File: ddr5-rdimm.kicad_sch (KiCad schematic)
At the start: 31 parts, among them J2 Bus_DDR5_DDR504111002KQ, Q10 BSS138PW, Q11 BSS138PW, Q9 BSS138PW, SW3 SW_KMR211NGLFS_SMD

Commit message: [#65754] Rename project
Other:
- title: SO-DIMM DDR5 Tester -> RDIMM DDR5 Tester

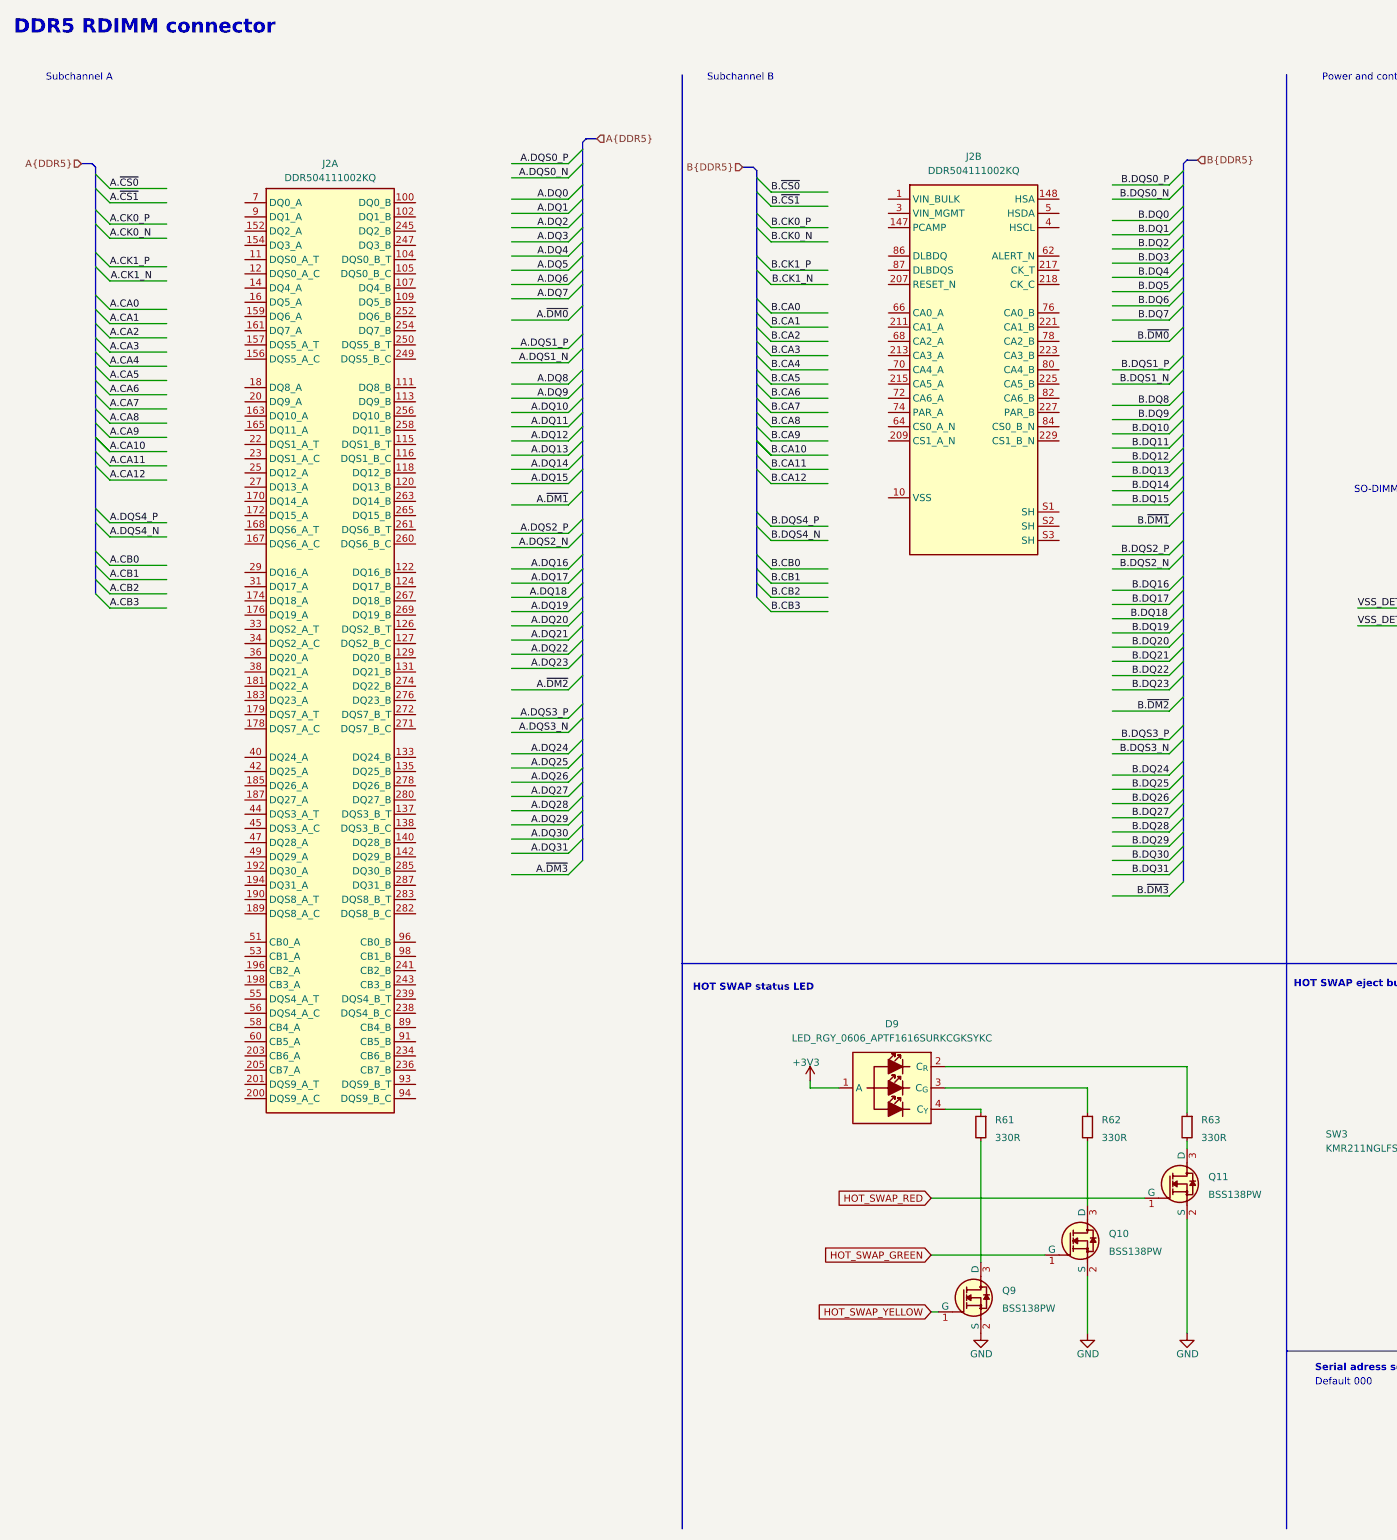
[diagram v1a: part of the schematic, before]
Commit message: [#66521] Connect labels to DDR5 connector - define DDR5_RDIMM bus
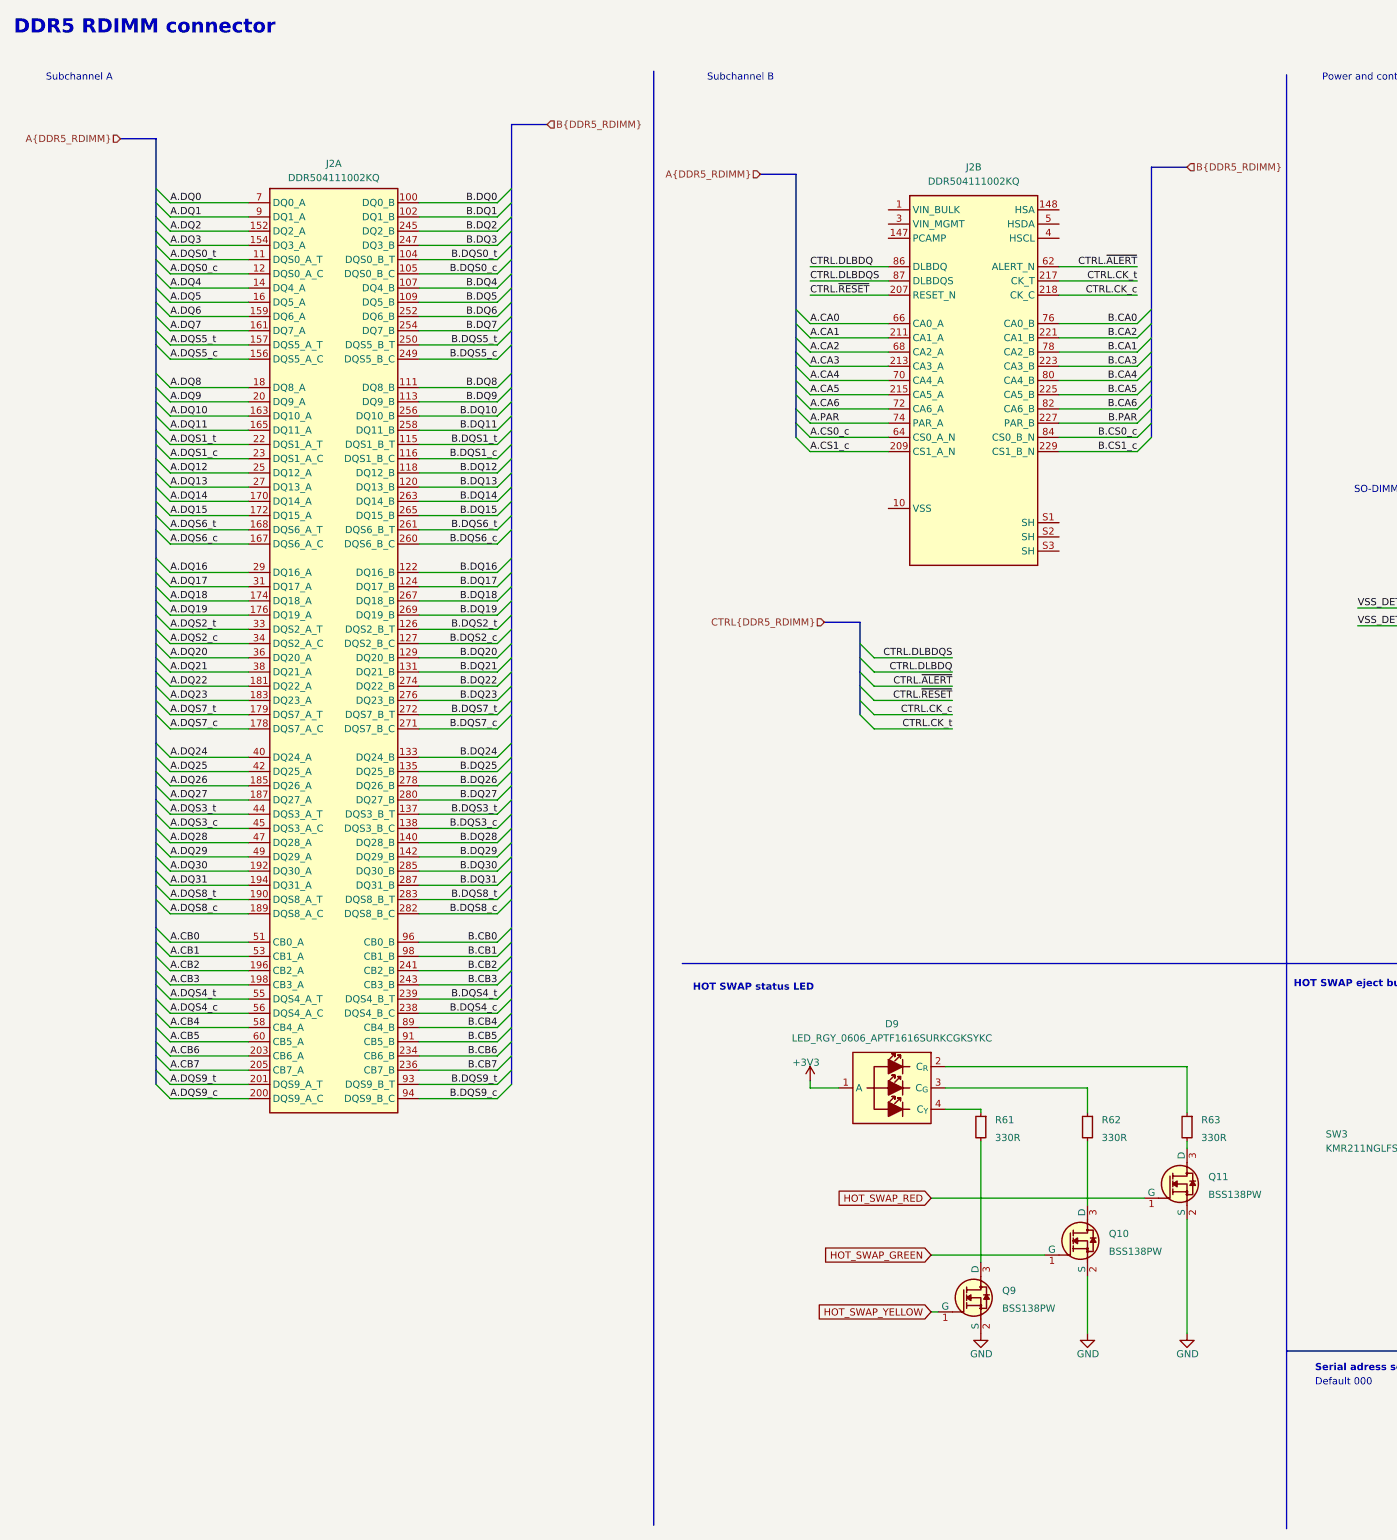
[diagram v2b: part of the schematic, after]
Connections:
- net A.CA0: now also J2.66 (CA0_A)
- net A.CA1: now also J2.211 (CA1_A)
- net A.CA2: now also J2.68 (CA2_A)
- net A.CA3: now also J2.213 (CA3_A)
- net A.CA4: now also J2.70 (CA4_A)
- net A.CA5: now also J2.215 (CA5_A)
- net A.CA6: now also J2.72 (CA6_A)
- net A.CB0: now also J2.51 (CB0_A)
- net A.CB1: now also J2.53 (CB1_A)
- net A.CB2: now also J2.196 (CB2_A)
- net A.CB3: now also J2.198 (CB3_A)
- net A.DQ0: now also J2.7 (DQ0_A)
- net A.DQ1: now also J2.9 (DQ1_A)
- net A.DQ10: now also J2.163 (DQ10_A)
- net A.DQ11: now also J2.165 (DQ11_A)
- net A.DQ12: now also J2.25 (DQ12_A)
- net A.DQ13: now also J2.27 (DQ13_A)
- net A.DQ14: now also J2.170 (DQ14_A)
- net A.DQ15: now also J2.172 (DQ15_A)
- net A.DQ16: now also J2.29 (DQ16_A)
- net A.DQ17: now also J2.31 (DQ17_A)
- net A.DQ18: now also J2.174 (DQ18_A)
- net A.DQ19: now also J2.176 (DQ19_A)
- net A.DQ2: now also J2.152 (DQ2_A)
- net A.DQ20: now also J2.36 (DQ20_A)
- net A.DQ21: now also J2.38 (DQ21_A)
- net A.DQ22: now also J2.181 (DQ22_A)
- net A.DQ23: now also J2.183 (DQ23_A)
- net A.DQ24: now also J2.40 (DQ24_A)
- net A.DQ25: now also J2.42 (DQ25_A)
- net A.DQ26: now also J2.185 (DQ26_A)
- net A.DQ27: now also J2.187 (DQ27_A)
- net A.DQ28: now also J2.47 (DQ28_A)
- net A.DQ29: now also J2.49 (DQ29_A)
- net A.DQ3: now also J2.154 (DQ3_A)
- net A.DQ30: now also J2.192 (DQ30_A)
- net A.DQ31: now also J2.194 (DQ31_A)
- net A.DQ4: now also J2.14 (DQ4_A)
- net A.DQ5: now also J2.16 (DQ5_A)
- net A.DQ6: now also J2.159 (DQ6_A)
- net A.DQ7: now also J2.161 (DQ7_A)
- net A.DQ8: now also J2.18 (DQ8_A)
- net A.DQ9: now also J2.20 (DQ9_A)
- net B.CA0: now also J2.76 (CA0_B)
- net B.CA1: now also J2.78 (CA2_B)
- net B.CA2: now also J2.221 (CA1_B)
- net B.CA3: now also J2.223 (CA3_B)
- net B.CA4: now also J2.80 (CA4_B)
- net B.CA5: now also J2.225 (CA5_B)
- net B.CA6: now also J2.82 (CA6_B)
- net B.CB0: now also J2.96 (CB0_B)
- net B.CB1: now also J2.98 (CB1_B)
- net B.CB2: now also J2.241 (CB2_B)
- net B.CB3: now also J2.243 (CB3_B)
- net B.DQ0: now also J2.100 (DQ0_B)
- net B.DQ1: now also J2.102 (DQ1_B)
- net B.DQ10: now also J2.256 (DQ10_B)
- net B.DQ11: now also J2.258 (DQ11_B)
- net B.DQ12: now also J2.118 (DQ12_B)
- net B.DQ13: now also J2.120 (DQ13_B)
- net B.DQ14: now also J2.263 (DQ14_B)
- net B.DQ15: now also J2.265 (DQ15_B)
- net B.DQ16: now also J2.122 (DQ16_B)
- net B.DQ17: now also J2.124 (DQ17_B)
- net B.DQ18: now also J2.267 (DQ18_B)
- net B.DQ19: now also J2.269 (DQ19_B)
- net B.DQ2: now also J2.245 (DQ2_B)
- net B.DQ20: now also J2.129 (DQ20_B)
- net B.DQ21: now also J2.131 (DQ21_B)
- net B.DQ22: now also J2.274 (DQ22_B)
- net B.DQ23: now also J2.276 (DQ23_B)
- net B.DQ24: now also J2.133 (DQ24_B)
- net B.DQ25: now also J2.135 (DQ25_B)
- net B.DQ26: now also J2.278 (DQ26_B)
- net B.DQ27: now also J2.280 (DQ27_B)
- net B.DQ28: now also J2.140 (DQ28_B)
- net B.DQ29: now also J2.142 (DQ29_B)
- net B.DQ3: now also J2.247 (DQ3_B)
- net B.DQ30: now also J2.285 (DQ30_B)
- net B.DQ31: now also J2.287 (DQ31_B)
- net B.DQ4: now also J2.107 (DQ4_B)
- net B.DQ5: now also J2.109 (DQ5_B)
- net B.DQ6: now also J2.252 (DQ6_B)
- net B.DQ7: now also J2.254 (DQ7_B)
- net B.DQ8: now also J2.111 (DQ8_B)
- net B.DQ9: now also J2.113 (DQ9_B)
- net B.DQS0_t: now reaches J2.104 (DQS0_B_T)
- net B.DQS0_c: now reaches J2.105 (DQS0_B_C)
- net A.DQS0_t: now reaches J2.11 (DQS0_A_T)
- net B.DQS1_t: now reaches J2.115 (DQS1_B_T)
- net B.DQS1_c: now reaches J2.116 (DQS1_B_C)
- net A.DQS0_c: now reaches J2.12 (DQS0_A_C)
- net B.DQS2_t: now reaches J2.126 (DQS2_B_T)
- net B.DQS2_c: now reaches J2.127 (DQS2_B_C)
- net B.DQS3_t: now reaches J2.137 (DQS3_B_T)
- net B.DQS3_c: now reaches J2.138 (DQS3_B_C)
- net A.DQS5_c: now reaches J2.156 (DQS5_A_C)
- net A.DQS5_t: now reaches J2.157 (DQS5_A_T)
- net A.DQS6_c: now reaches J2.167 (DQS6_A_C)
- net A.DQS6_t: now reaches J2.168 (DQS6_A_T)
- net A.DQS7_c: now reaches J2.178 (DQS7_A_C)
- net A.DQS7_t: now reaches J2.179 (DQS7_A_T)
- net A.DQS8_c: now reaches J2.189 (DQS8_A_C)
- net A.DQS8_t: now reaches J2.190 (DQS8_A_T)
- net A.DQS9_c: now reaches J2.200 (DQS9_A_C)
- net A.DQS9_t: now reaches J2.201 (DQS9_A_T)
- net A.CB6: now reaches J2.203 (CB6_A)
- net A.CB7: now reaches J2.205 (CB7_A)
- net A.DQS1_t: now reaches J2.22 (DQS1_A_T)
- net A.DQS1_c: now reaches J2.23 (DQS1_A_C)
- net B.CB6: now reaches J2.234 (CB6_B)
- net B.CB7: now reaches J2.236 (CB7_B)
- net B.DQS4_c: now reaches J2.238 (DQS4_B_C)
- net B.DQS4_t: now reaches J2.239 (DQS4_B_T)
- net B.DQS5_c: now reaches J2.249 (DQS5_B_C)
- net B.DQS5_t: now reaches J2.250 (DQS5_B_T)
- net B.DQS6_c: now reaches J2.260 (DQS6_B_C)
- net B.DQS6_t: now reaches J2.261 (DQS6_B_T)
- net B.DQS7_c: now reaches J2.271 (DQS7_B_C)
- net B.DQS7_t: now reaches J2.272 (DQS7_B_T)
- net B.DQS8_c: now reaches J2.282 (DQS8_B_C)
- net B.DQS8_t: now reaches J2.283 (DQS8_B_T)
- net A.DQS2_t: now reaches J2.33 (DQS2_A_T)
- net A.DQS2_c: now reaches J2.34 (DQS2_A_C)
- net A.DQS3_t: now reaches J2.44 (DQS3_A_T)
- net A.DQS3_c: now reaches J2.45 (DQS3_A_C)
- net A.DQS4_t: now reaches J2.55 (DQS4_A_T)
- net A.DQS4_c: now reaches J2.56 (DQS4_A_C)
- net A.CB4: now reaches J2.58 (CB4_A)
- net A.CB5: now reaches J2.60 (CB5_A)
- net B.CB4: now reaches J2.89 (CB4_B)
- net B.CB5: now reaches J2.91 (CB5_B)
- net B.DQS9_t: now reaches J2.93 (DQS9_B_T)
- net B.DQS9_c: now reaches J2.94 (DQS9_B_C)
- net CTRL.~{RESET}: now reaches J2.207 (RESET_N)
- net A.CS1_c: now reaches J2.209 (CS1_A_N)
- net CTRL.CK_t: now reaches J2.217 (CK_T)
- net CTRL.CK_c: now reaches J2.218 (CK_C)
- net B.PAR: now reaches J2.227 (PAR_B)
- net B.CS1_c: now reaches J2.229 (CS1_B_N)
- net CTRL.~{ALERT}: now reaches J2.62 (ALERT_N)
- net A.CS0_c: now reaches J2.64 (CS0_A_N)
- net A.PAR: now reaches J2.74 (PAR_A)
- net B.CS0_c: now reaches J2.84 (CS0_B_N)
- net CTRL.DLBDQ: now reaches J2.86 (DLBDQ)
- net CTRL.DLBDQS: now reaches J2.87 (DLBDQS)
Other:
- moved on the sheet: J2A, J2B

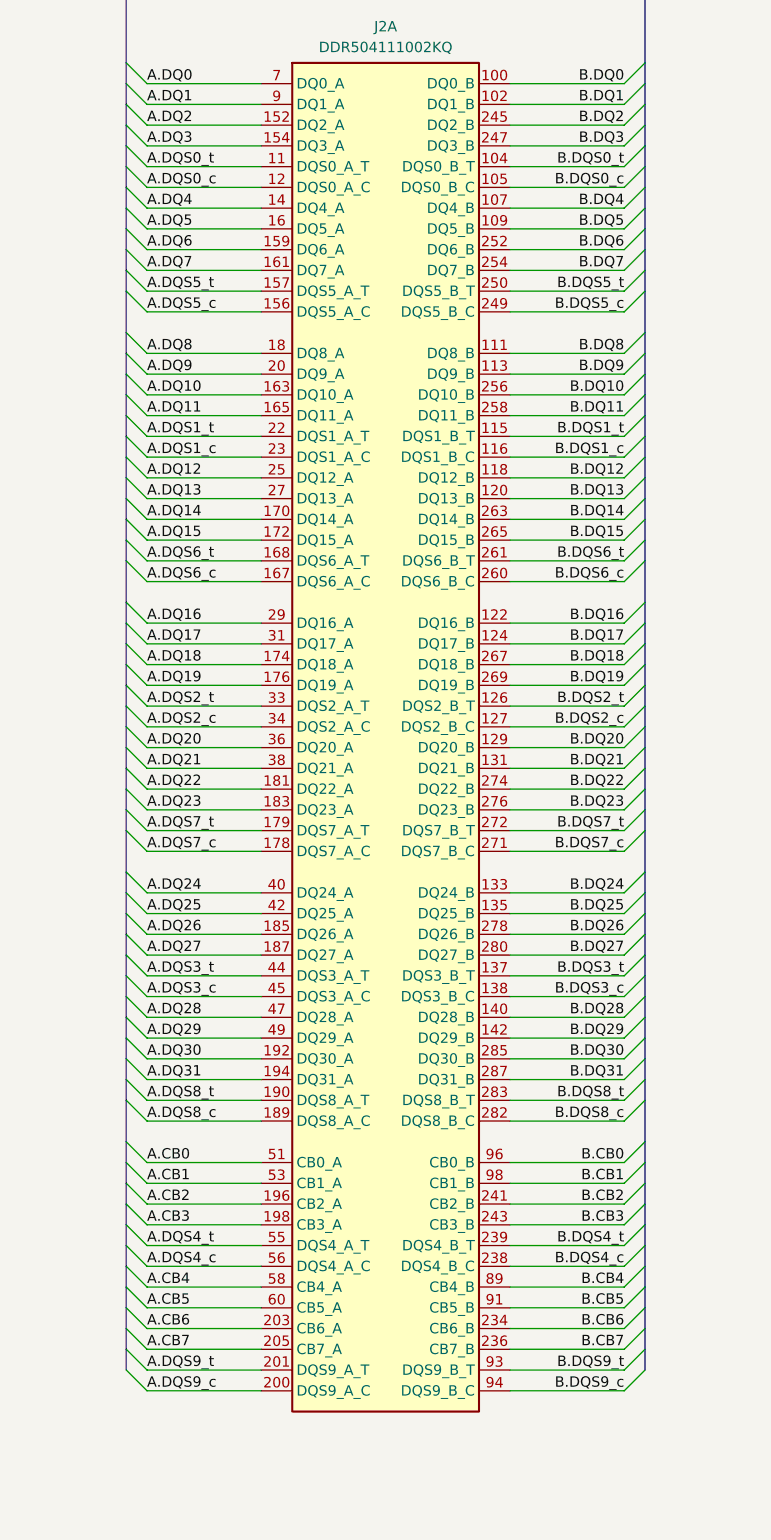
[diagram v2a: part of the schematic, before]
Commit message: [#66521] Rename DQS pairs
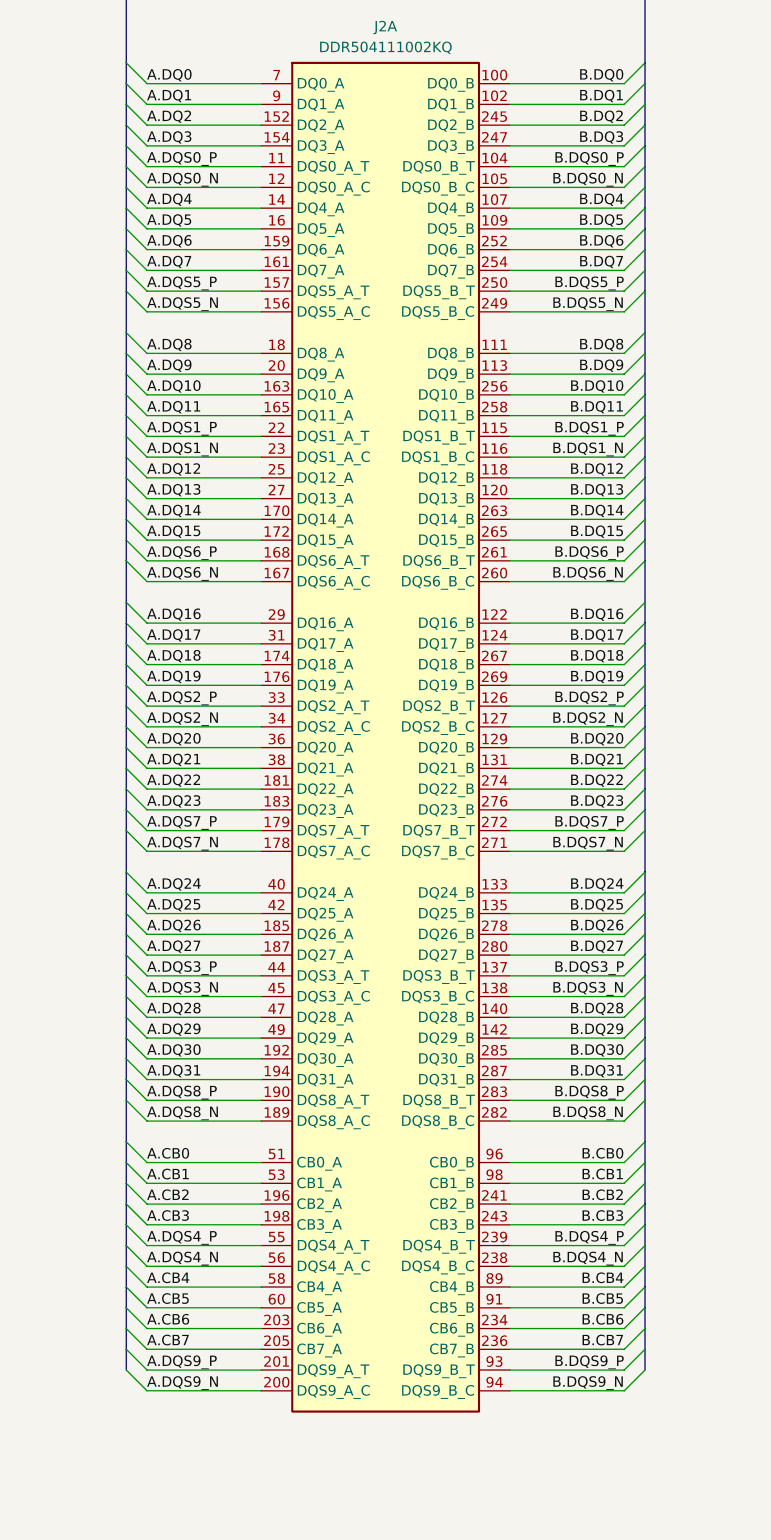
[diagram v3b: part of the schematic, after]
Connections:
- net A.DQS0_c renamed A.DQS0_N
- net A.DQS0_t renamed A.DQS0_P
- net A.DQS1_c renamed A.DQS1_N
- net A.DQS1_t renamed A.DQS1_P
- net A.DQS2_c renamed A.DQS2_N
- net A.DQS2_t renamed A.DQS2_P
- net A.DQS3_c renamed A.DQS3_N
- net A.DQS3_t renamed A.DQS3_P
- net A.DQS4_c renamed A.DQS4_N
- net A.DQS4_t renamed A.DQS4_P
- net A.DQS5_c renamed A.DQS5_N
- net A.DQS5_t renamed A.DQS5_P
- net A.DQS6_c renamed A.DQS6_N
- net A.DQS6_t renamed A.DQS6_P
- net A.DQS7_c renamed A.DQS7_N
- net A.DQS7_t renamed A.DQS7_P
- net A.DQS8_c renamed A.DQS8_N
- net A.DQS8_t renamed A.DQS8_P
- net A.DQS9_c renamed A.DQS9_N
- net A.DQS9_t renamed A.DQS9_P
- net B.DQS0_c renamed B.DQS0_N
- net B.DQS0_t renamed B.DQS0_P
- net B.DQS1_c renamed B.DQS1_N
- net B.DQS1_t renamed B.DQS1_P
- net B.DQS2_c renamed B.DQS2_N
- net B.DQS2_t renamed B.DQS2_P
- net B.DQS3_c renamed B.DQS3_N
- net B.DQS3_t renamed B.DQS3_P
- net B.DQS4_c renamed B.DQS4_N
- net B.DQS4_t renamed B.DQS4_P
- net B.DQS5_c renamed B.DQS5_N
- net B.DQS5_t renamed B.DQS5_P
- net B.DQS6_c renamed B.DQS6_N
- net B.DQS6_t renamed B.DQS6_P
- net B.DQS7_c renamed B.DQS7_N
- net B.DQS7_t renamed B.DQS7_P
- net B.DQS8_c renamed B.DQS8_N
- net B.DQS8_t renamed B.DQS8_P
- net B.DQS9_c renamed B.DQS9_N
- net B.DQS9_t renamed B.DQS9_P
